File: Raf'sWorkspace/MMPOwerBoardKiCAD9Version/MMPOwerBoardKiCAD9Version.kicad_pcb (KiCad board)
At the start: 2 copper layers, 105 parts, among them J1 TYPE-C-31-M-04, J2 Conn_02x16_Odd_Even, J3 Conn_01x02, Q1 SS8050, SW1 SS-12D11-G050, U1 HUSB237, U10 TPS22917DBVR, U11 AMS1117-5.0, U2 TP4056-42-ESOP8, U3 DRV8833PWPR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

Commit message: Organised PCB on recommended board size
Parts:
- removed the R2 at (147.2, -95.5)
- moved TP17 256.7 mm to (201.9, 87.7)
- moved SW1 181.2 mm to (236.3, 84.0), turned to -90 degrees
- moved C13 175.0 mm to (235.0, 56.8)
- moved C14 175.0 mm to (234.5, 59.5)
- moved L2 175.0 mm to (238.8, 56.5)
- moved L3 175.0 mm to (238.8, 61.0)
- moved R14 175.0 mm to (231.0, 59.5)
- moved R15 175.0 mm to (230.0, 56.0)
- moved R16 175.0 mm to (233.5, 52.5)
- moved U4 175.0 mm to (232.9, 57.0)
- moved R34 169.0 mm to (212.9, 93.2)
- moved C4 168.6 mm to (222.0, 86.5)
- moved C5 168.6 mm to (220.0, 86.6)
- moved C6 168.6 mm to (220.0, 83.4)
- moved R3 168.6 mm to (207.9, 84.7)
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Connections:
- R14 pad 2: Net-(JP2-A) -> Net-(U4-FB)
- R15 pad 1: Net-(JP2-A) -> Net-(U4-FB)
- R16 pad 2: Net-(JP2-A) -> Net-(U4-PG)
- TP11 pad 1: Net-(JP2-A) -> Net-(U4-FB)
- U4 pad 4: Net-(JP2-A) -> Net-(U4-FB)
- U4 pad 5: Net-(JP2-A) -> Net-(U4-PG)

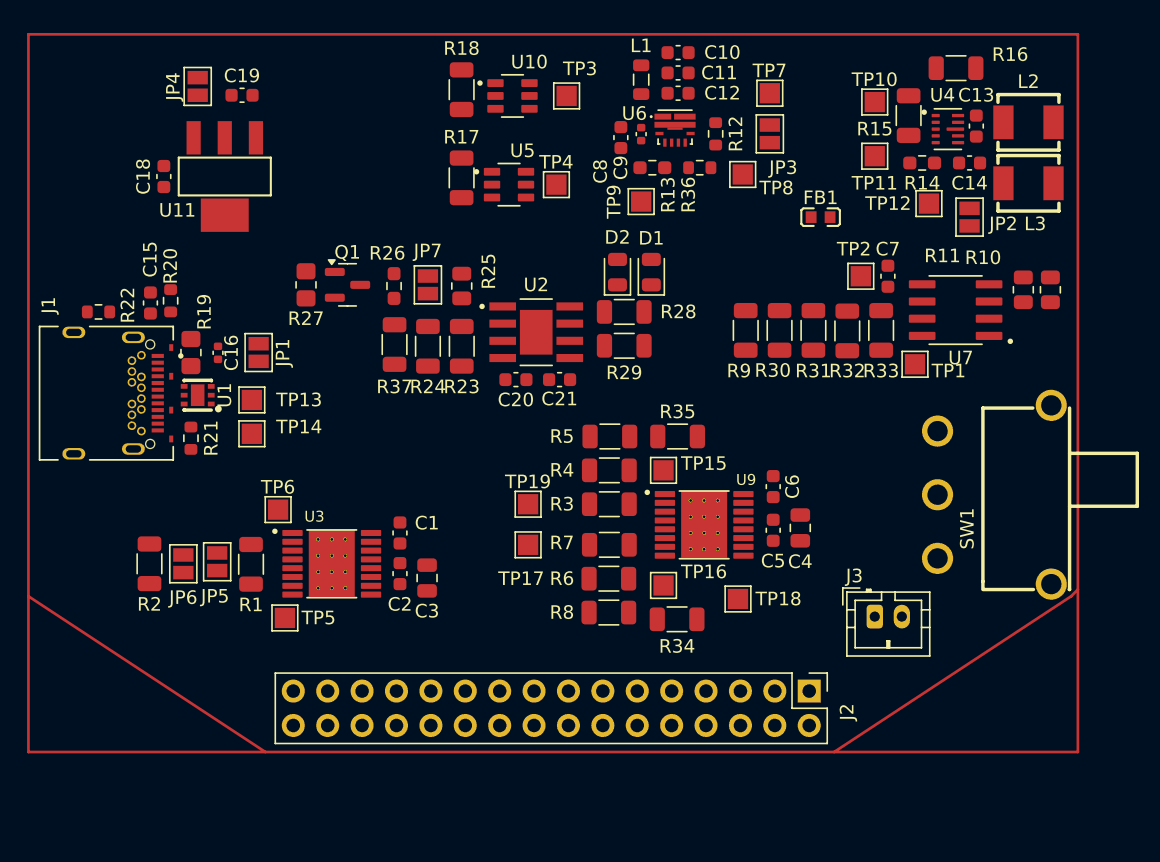
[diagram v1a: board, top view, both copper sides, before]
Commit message: Added all tracks
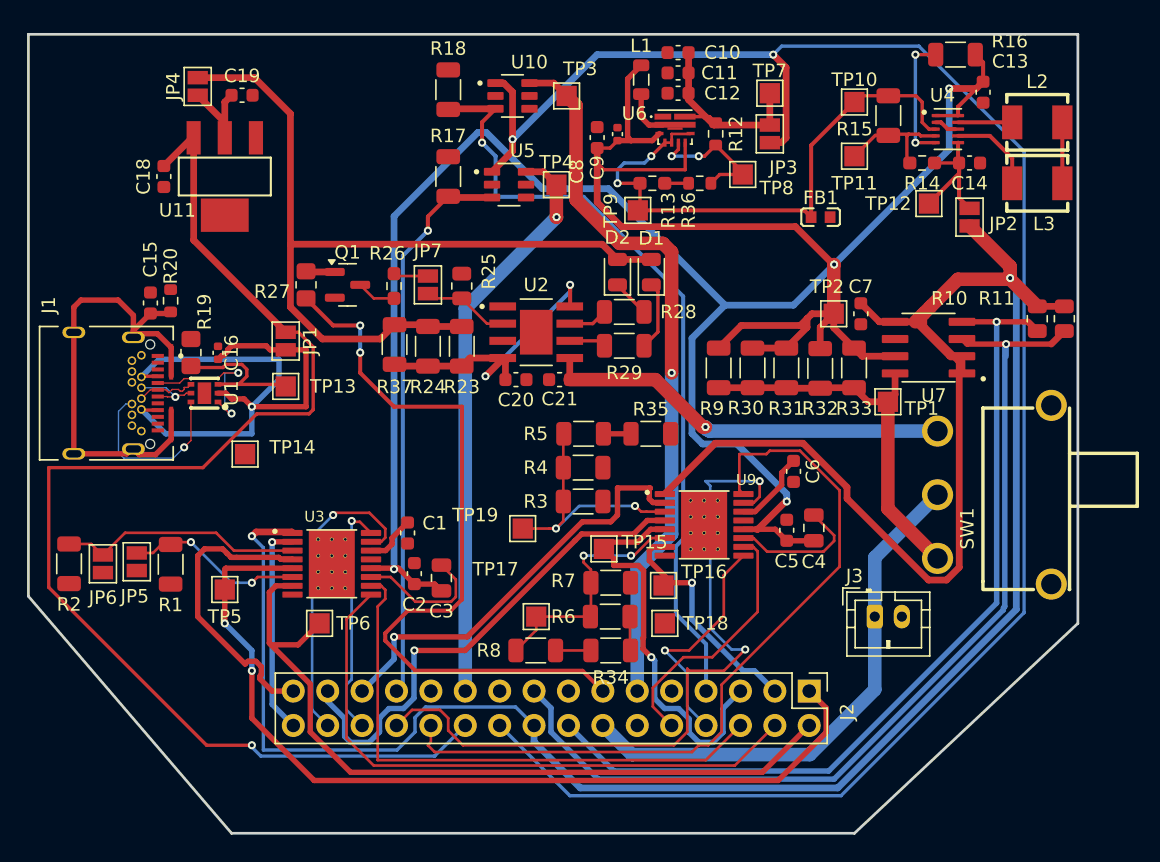
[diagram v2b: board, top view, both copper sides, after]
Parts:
- removed R21, R22: 1M, Resistor_SMD:R_0603_1608Metric
- moved TP6 8.94 mm to (186.5, 93.5)
- moved TP15 7.28 mm to (207.5, 88.0)
- moved R8 6.08 mm to (202.5, 95.5)
- moved JP5 5.94 mm to (173.0, 89.0)
- moved JP6 5.94 mm to (170.5, 89.1)
- moved R1 5.94 mm to (175.5, 89.1)
- moved R2 5.94 mm to (168.0, 89.1)
- moved TP18 5.69 mm to (212.0, 93.5)
- moved R34 5.41 mm to (208.0, 95.5)
- moved TP17 5.33 mm to (202.5, 93.0)
- moved TP5 4.91 mm to (179.5, 91.0)
- moved R11 3.71 mm to (241.5, 71.0)
- moved C7 3.42 mm to (226.5, 70.6)
- moved R30 3.42 mm to (218.5, 74.6)
- moved R31 3.42 mm to (221.0, 74.6)
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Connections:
- J1 pad A8: Net-(J1-SUB1) -> unconnected-(J1-SUB1-PadA8)
- J1 pad B8: Net-(J1-SUB2) -> unconnected-(J1-SUB2-PadB8)
- R3 pad 2: Net-(R3-Pad2) -> GND
- R34 pad 2: Net-(R34-Pad2) -> GND
- R35 pad 2: Net-(R3-Pad2) -> GND
- R6 pad 2: Net-(R34-Pad2) -> GND
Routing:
- net /LoadCircuit: track 0.00 -> 201.5 mm, vias 0 -> 4
- net /3V3: track 0.00 -> 187.0 mm, vias 0 -> 2
- net /5V: track 0.00 -> 140.3 mm, vias 0 -> 2
- net /9V: track 0.00 -> 94.4 mm, vias 0 -> 1
- net /I2C1_SDA: track 0.00 -> 71.4 mm, vias 0 -> 1
- net /Motor2_B_OUT: track 0.00 -> 66.2 mm, vias 0 -> 2
- net /I2C1_SCL: track 0.00 -> 64.8 mm, vias 0 -> 1
- net /5V_charge: track 0.00 -> 63.5 mm
- net /EXT_LOAD2_CTRL: track 0.00 -> 58.0 mm, vias 0 -> 1
- net /MOTOR3_CTRL1: track 0.00 -> 57.3 mm
- net /Motor2_A_OUT: track 0.00 -> 57.2 mm
- net /FAST_CHARGE_CTRL: track 0.00 -> 56.0 mm, vias 0 -> 2
- net /MOTOR3_CTRL2: track 0.00 -> 54.4 mm, vias 0 -> 2
- net /EXT_LOAD2_OUT: track 0.00 -> 53.2 mm, vias 0 -> 1
- net Net-(JP1-B): track 0.00 -> 46.5 mm, vias 0 -> 1
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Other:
- board outline added: 77.5 x 59 mm

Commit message: PCB seems to be done - BOM also generated
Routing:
- net GND: track 4.17 -> 206.9 mm, vias 0 -> 22
- net /5V: track 140.3 -> 144.2 mm
- net Net-(JP1-B): track 46.5 -> 49.4 mm
- net /5V_charge: track 63.5 -> 64.6 mm
- net Net-(J1-CC2): track 13.2 -> 14.3 mm
- net /9V: track 94.4 -> 95.1 mm
- net Net-(U4-L2): track 6.53 -> 5.92 mm
- added copper zone on B.Cu, net GND
- added copper zone on F.Cu, net GND
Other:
- board size 77.5 x 59 mm -> 79 x 60 mm

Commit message: GTFO Finished
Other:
- board text added: "CRDRAF001 DLLAMI004"
- board text added: "Group 6"
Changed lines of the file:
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@@
 		(layer "Edge.Cuts")
+	)
+	(gr_text "Group 6"
+		(at 165.5 56.5 0)
+		(layer "F.SilkS")
+		(effects
+			(font
+				(size 1.5 1.5)
+				(thickness 0.3)
+				(bold yes)
+			)
+			(justify left bottom)
+		)
+	)
+	(gr_text "CRDRAF001\nDLLAMI004"
+		(at 165.5 53.5 0)
+		(layer "F.SilkS")
+		(effects
+			(font
+				(size 1 1)
+				(thickness 0.25)
+				(bold yes)
+			)
+			(justify left bottom)
+		)
 	)
 	(segment

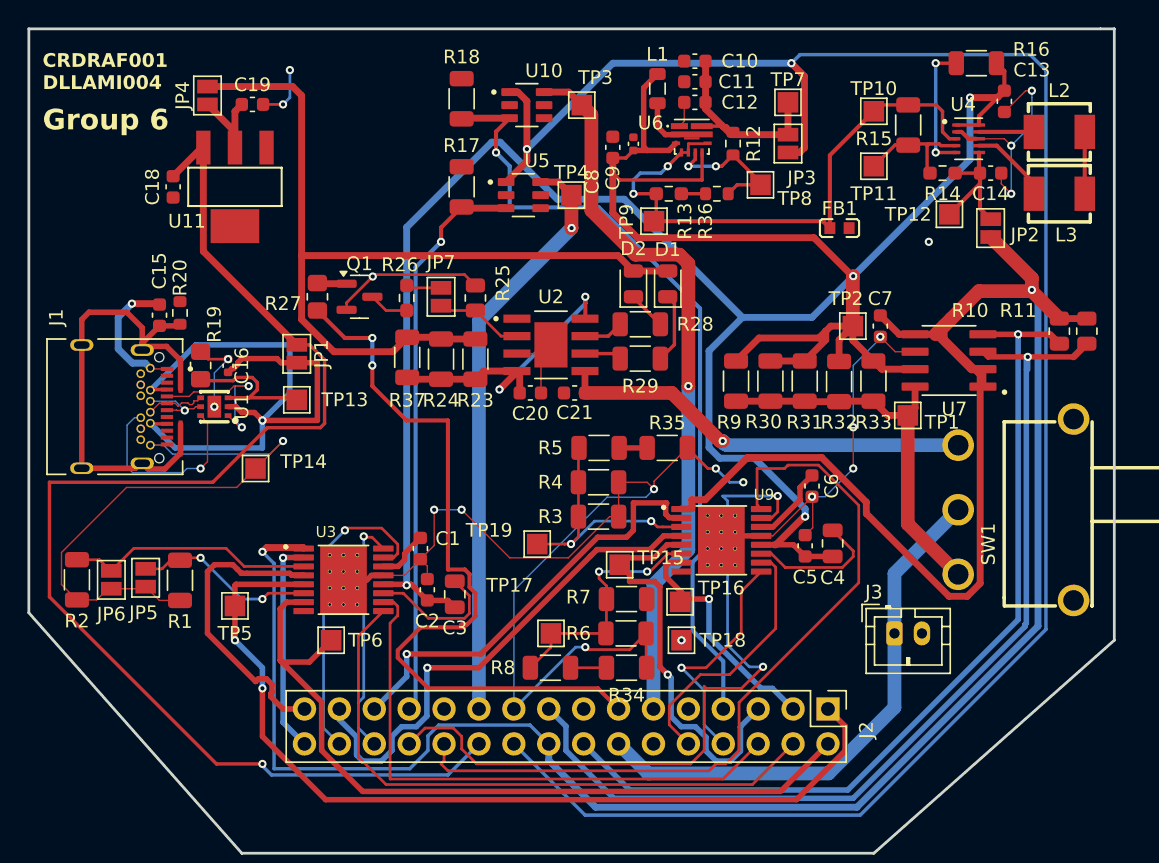
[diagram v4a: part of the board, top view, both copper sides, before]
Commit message: A few minor changes to improve results on rule checker: 0,1mm adjusted to 0,15mm, regions of silkscreen on pad were removed
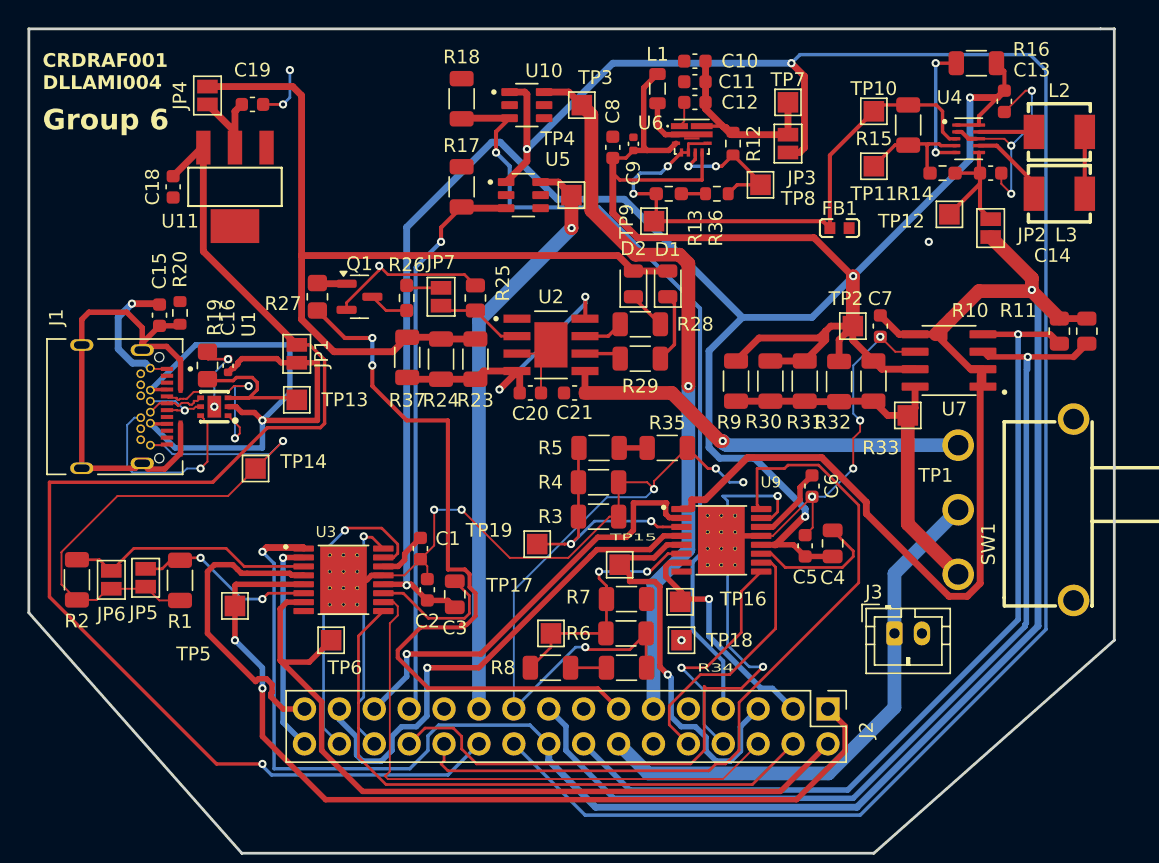
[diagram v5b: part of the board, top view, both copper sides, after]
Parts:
- moved R19 0.50 mm to (177.5, 73.5)
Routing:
- net /3V3: track 187.4 -> 183.7 mm
- net Net-(J1-CC1): track 11.8 -> 13.5 mm
- net GND: track 206.9 -> 208.0 mm

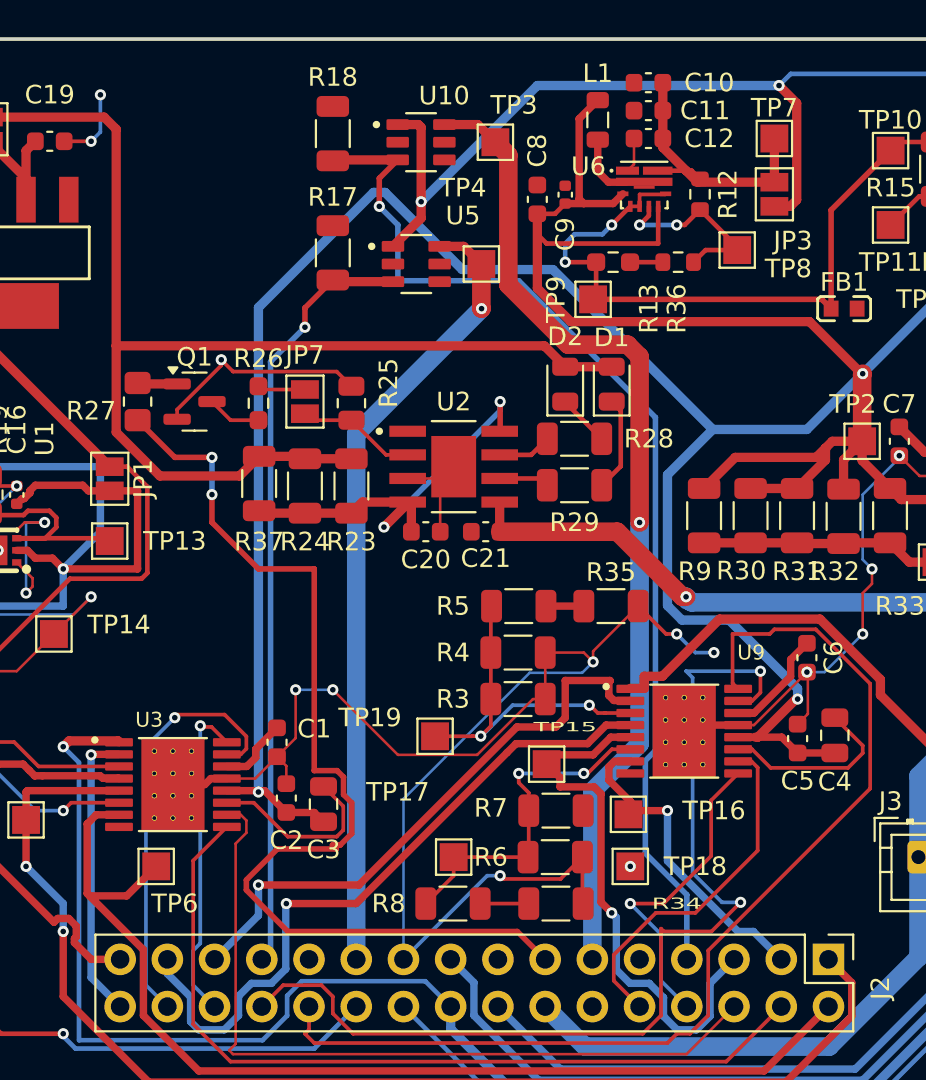
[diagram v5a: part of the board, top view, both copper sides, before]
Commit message: Added Drill hole space x1 to hold up board
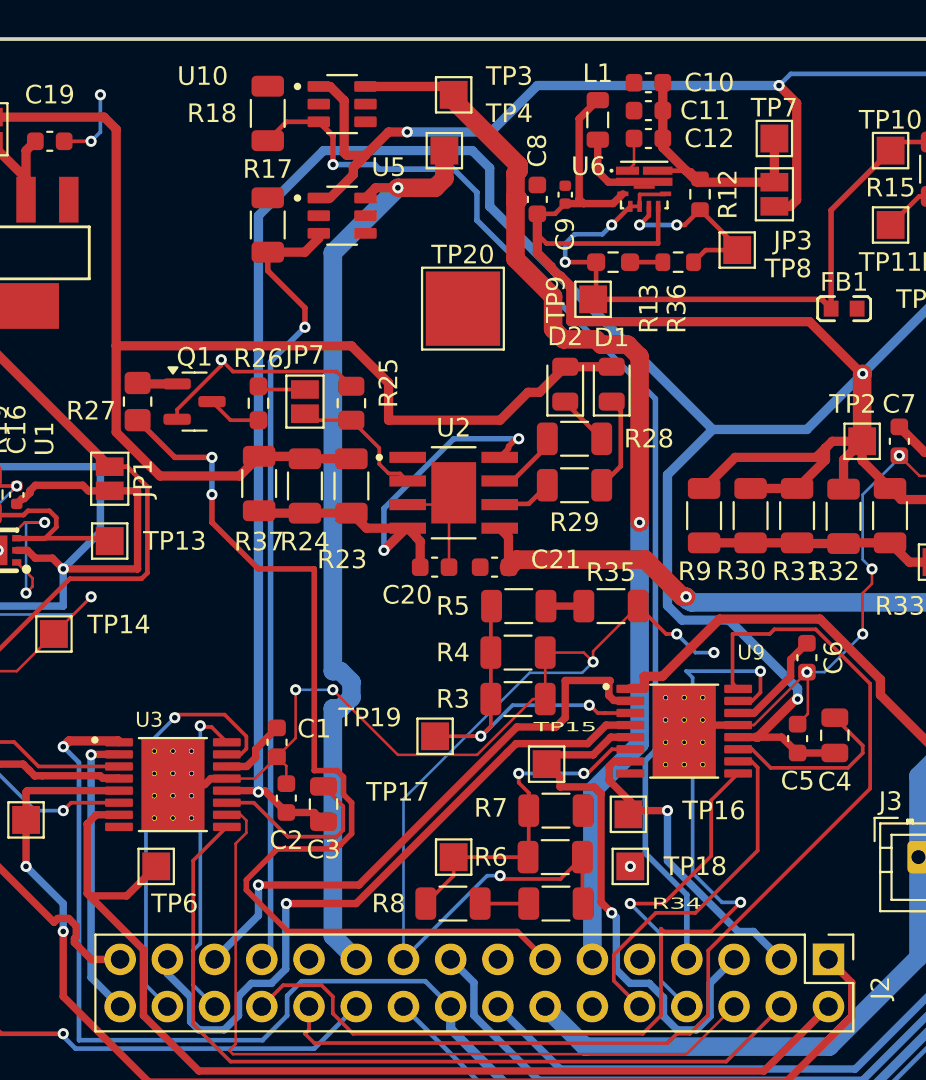
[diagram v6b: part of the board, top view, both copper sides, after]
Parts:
- added TP20: TestPoint, TestPoint:TestPoint_Pad_4.0x4.0mm, F.Cu at (203.0, 63.5)
- moved TP4 6.42 mm to (202.0, 55.0)
- moved U5 4.76 mm to (196.5, 58.5)
- moved U10 4.71 mm to (196.5, 52.5)
- moved R17 3.81 mm to (192.5, 59.0)
- moved R18 3.67 mm to (192.5, 53.0)
- moved TP3 3.40 mm to (202.5, 52.0)
- moved C20 1.96 mm to (201.5, 77.4)
- moved C21 1.96 mm to (204.7, 77.4)
- moved U2 1.41 mm to (202.5, 73.4)
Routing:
- net /EXT_LOAD1_OUT: track 42.8 -> 51.0 mm
- net /LoadCircuit: track 201.5 -> 207.5 mm
- net /EXT_LOAD2_OUT: track 53.2 -> 58.8 mm
- net /5V: track 144.5 -> 148.4 mm
- net /5V_charge: track 64.6 -> 68.2 mm
- net /EXT_LOAD2_CTRL: track 58.0 -> 60.5 mm
- net Net-(U2-CE): track 22.8 -> 25.1 mm
- net /EXT_LOAD1_CTRL: track 41.4 -> 43.1 mm
- net Net-(U2-~{CHRG}): track 2.92 -> 4.21 mm
- net Net-(JP7-B): track 6.44 -> 7.53 mm
- net Net-(U2-~{STDBY}): track 2.71 -> 3.55 mm
- net GND: track 208.0 -> 208.7 mm
